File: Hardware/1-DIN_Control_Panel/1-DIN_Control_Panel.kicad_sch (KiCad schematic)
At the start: 13 parts

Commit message: Schematic progress
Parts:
- added J1: Conn_01x06, symbol Connector_Generic:Conn_01x06
- added J3: Pot/SW - Brightness, symbol Connector_Generic:Conn_01x05
- added U2: AD8603, Package_TO_SOT_SMD:TSOT-23-5, symbol Amplifier_Operational:AD8603
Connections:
- net GND: now also J3.3 (B); no longer J?.2 (Pin_2)
- net at J?.1 (Pin_1): no longer J?.2 (Pin_2) (x3)
- net VCC renamed +BATT
- net +BATT: now also J3.1 (A)
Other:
- moved on the sheet: J?

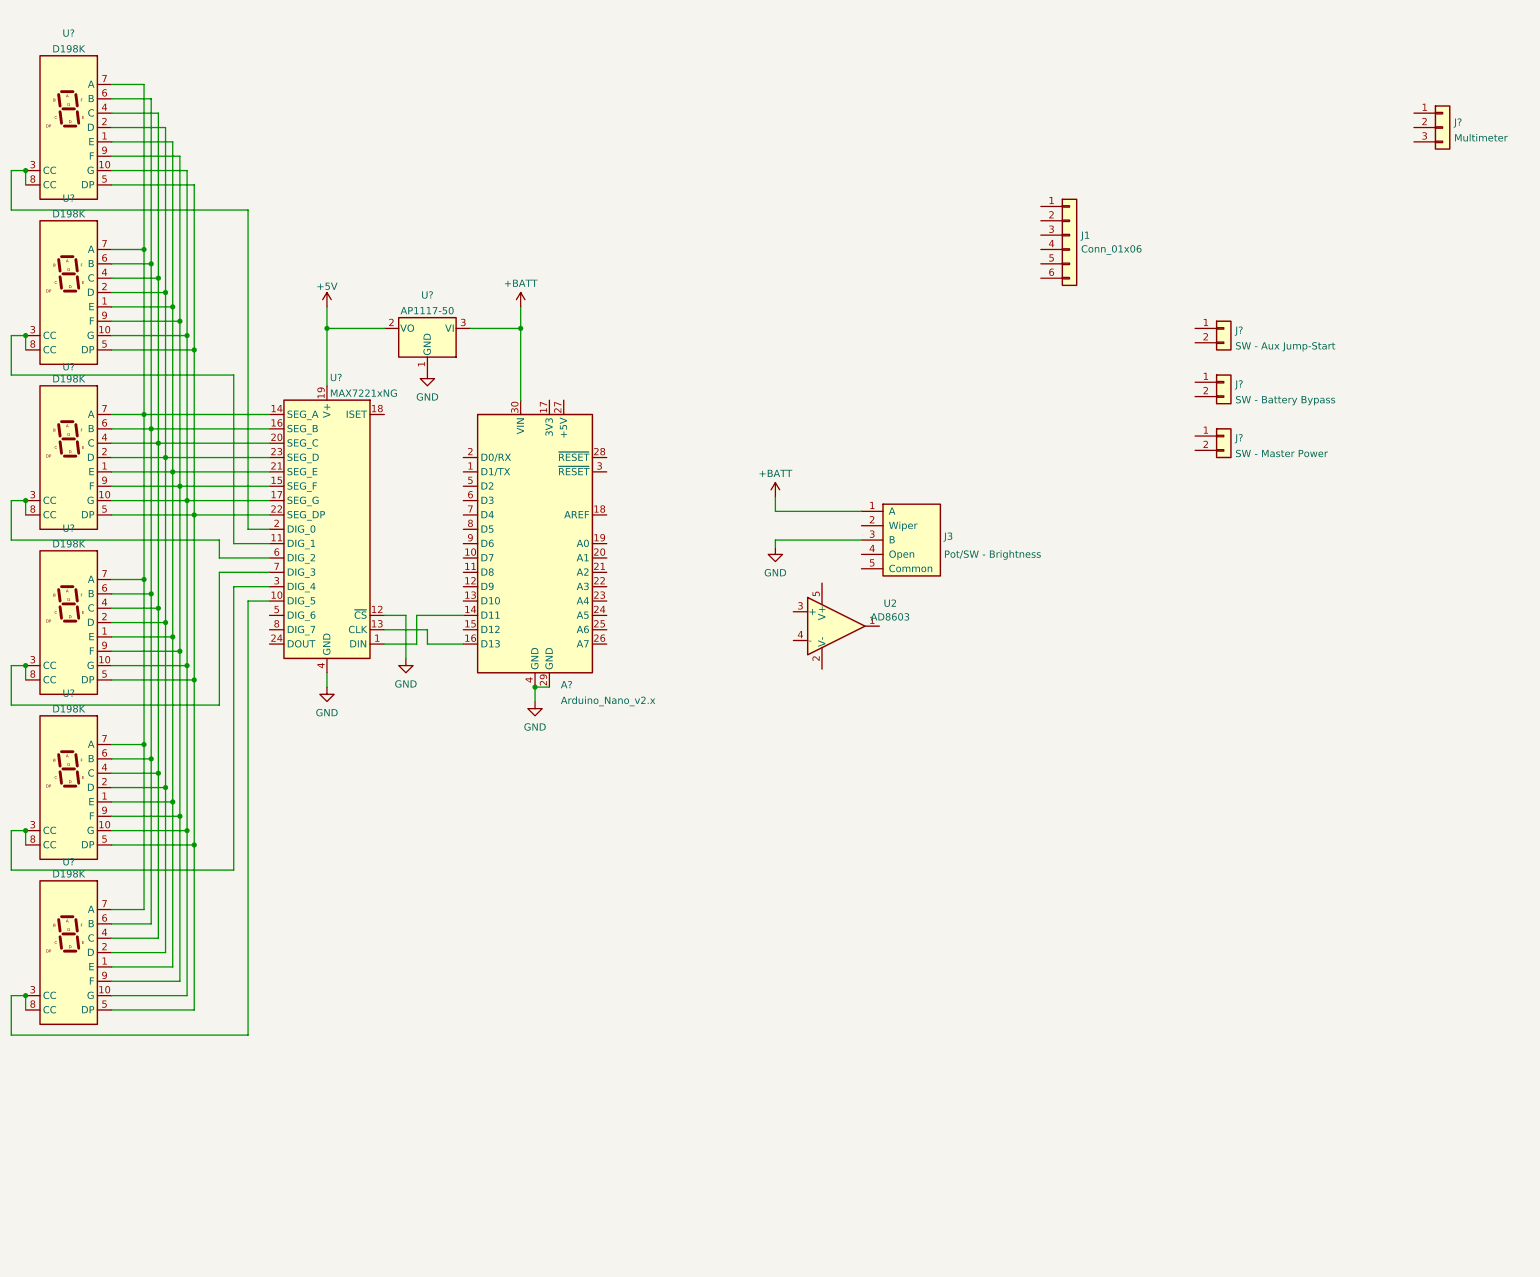
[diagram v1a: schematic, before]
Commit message: Added Instrumentation Amplifier To Schematic
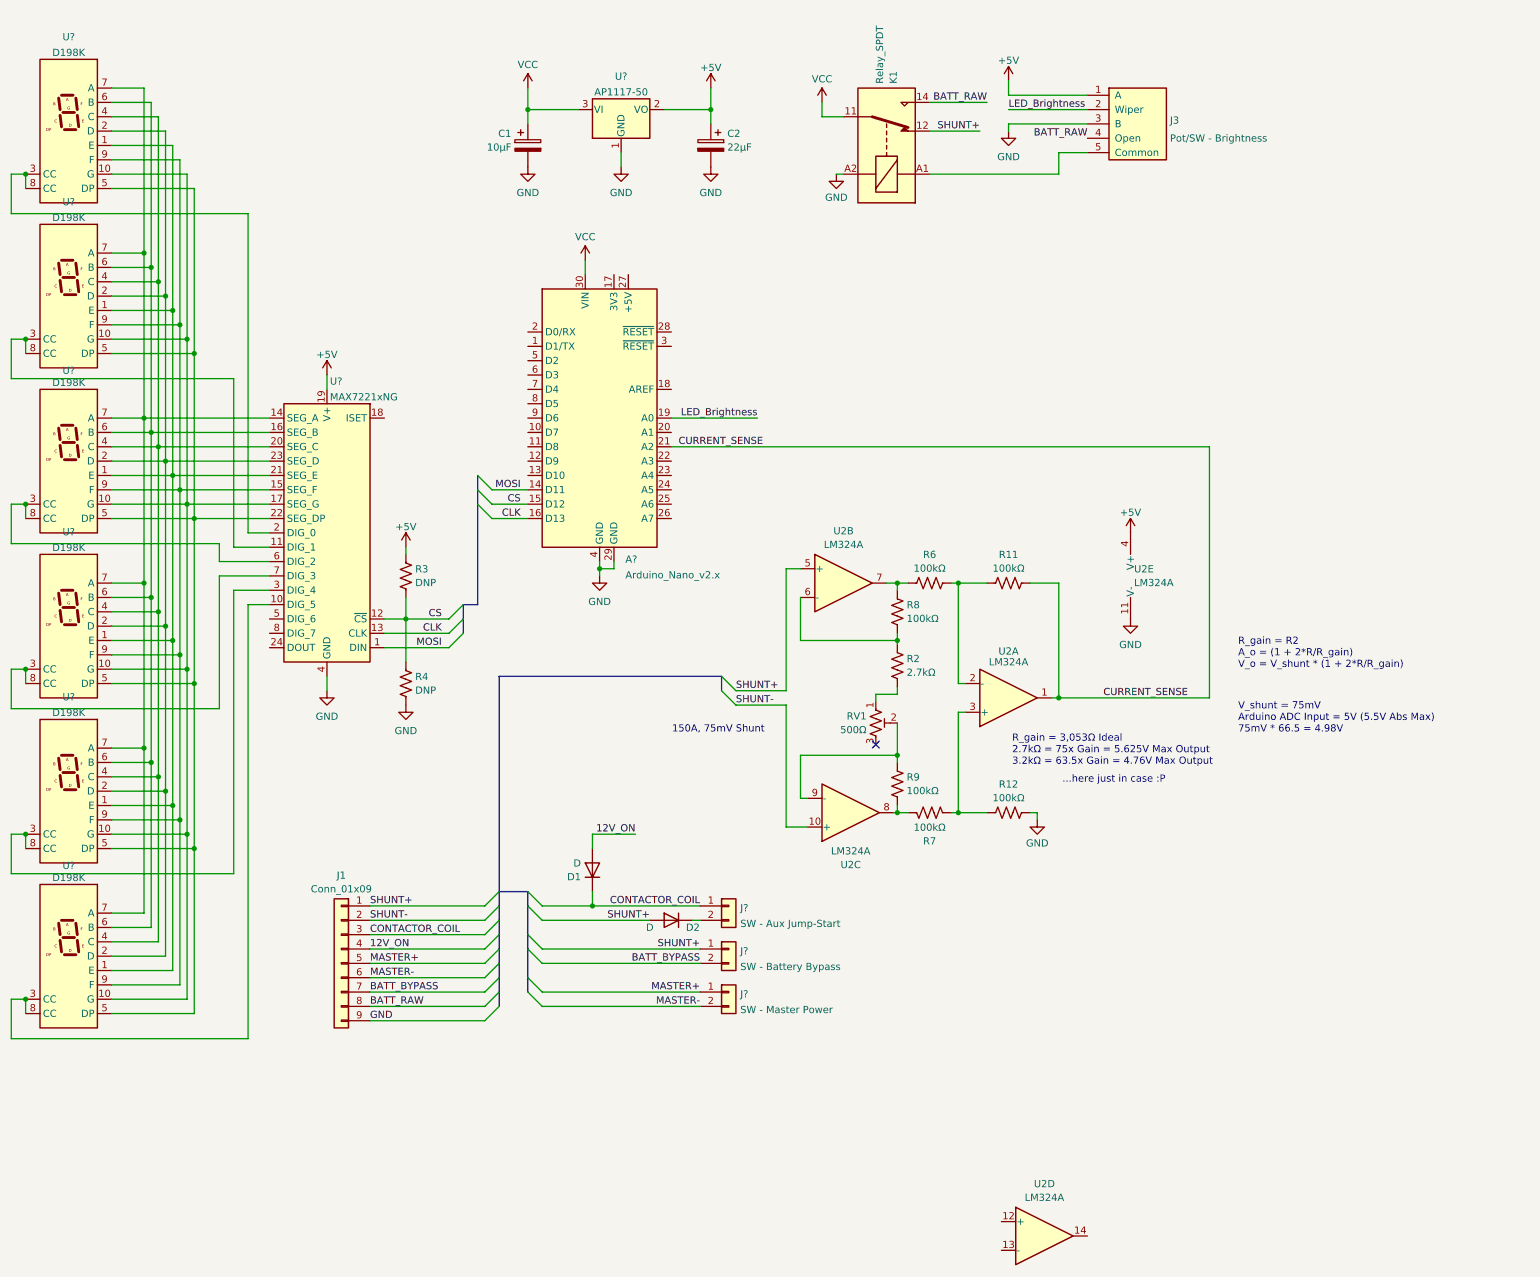
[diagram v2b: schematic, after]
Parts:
- removed J?: Multimeter, symbol Connector_Generic:Conn_01x03
- removed U2: AD8603, Package_TO_SOT_SMD:TSOT-23-5, symbol Amplifier_Operational:AD8603
- added C1: 10µF, symbol Device:C_Polarized
- added C2: 22µF, symbol Device:C_Polarized
- added D1, D2: D, symbol Device:D
- added K1: Relay_SPDT, symbol Relay:Relay_SPDT
- added R11, R12, R6, R7, R8, R9: 100kΩ, symbol Device:R_US
- added R2: 2.7kΩ, symbol Device:R_US
- added R3, R4: DNP, symbol Device:R_US
- added RV1: 500Ω, symbol Device:R_Potentiometer_Trim_US
- added U2: LM324A, symbol Amplifier_Operational:LM324A
- J1: value Conn_01x06 -> Conn_01x09; symbol Connector_Generic:Conn_01x06 -> Connector_Generic:Conn_01x09
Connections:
- net +5V: now also J3.1 (A), C2.1, R3.1, U2.4 (V+)
- net GND: now also J1.9 (Pin_9), C1.2, C2.2, K1.A2, R12.2, R4.2, U2.11 (V-); no longer U?.12 (~{CS})
- net SHUNT+: now reaches J1.1 (Pin_1)
- net SHUNT+: now also J?.1 (Pin_1), D2.2 (A), K1.12, U2.5 (+)
- net SHUNT-: now reaches J1.2 (Pin_2)
- net SHUNT-: now also U2.10 (+)
- net CONTACTOR_COIL: now reaches J1.3 (Pin_3)
- net CONTACTOR_COIL: now also J?.1 (Pin_1), D1.1 (K)
- net 12V_ON: now reaches J1.4 (Pin_4)
- net 12V_ON: now also D1.2 (A)
- net MASTER+: now reaches J1.5 (Pin_5)
- net MASTER+: now also J?.1 (Pin_1)
- net MASTER-: now reaches J1.6 (Pin_6)
- net MASTER-: now also J?.2 (Pin_2)
- net MOSI: now reaches A?.14 (D11), U?.1 (DIN)
- net CS: now reaches A?.15 (D12)
- net CS: now also U?.12 (~{CS}), R3.2, R4.1
- net CLK: now reaches A?.16 (D13), U?.13 (CLK)
- net LED_Brightness: now reaches A?.19 (A0)
- net LED_Brightness: now also J3.2 (Wiper)
- net CURRENT_SENSE: now reaches A?.21 (A2)
- net CURRENT_SENSE: now also R11.2, U2.1
- net BATT_BYPASS: now reaches J?.2 (Pin_2)
- net BATT_BYPASS: now also J1.7 (Pin_7)
- net at J?.2 (Pin_2): now also D2.1 (K)
- net BATT_RAW: now reaches J3.4 (Open)
- net BATT_RAW: now also J1.8 (Pin_8), K1.14
- net at J3.5 (Common): now also K1.A1
- net +BATT renamed VCC
- net VCC: now also C1.1, K1.11; no longer J3.1 (A)
- new net: R11.1, R6.2, U2.2 (-)
- new net: R12.1, R7.2, U2.3 (+)
- new net: R2.2, R8.1, U2.6 (-)
- new net: R6.1, R8.2, U2.7
- new net: R7.1, R9.1, U2.8
- new net: R9.2, RV1.2, U2.9 (-)
- new net: R2.1, RV1.1
- no-connect marks 0 -> 1
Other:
- note added: "...here just in case :P"
- note added: "150A, 75mV Shunt"
- note added: "R_gain = 3,053Ω Ideal 2.7kΩ = 75x Gain = 5.625V Max Output 3.2kΩ = 63.5x Gain = 4.76V Max Output"
- note added: "R_gain = R2 A_o = (1 + 2*R/R_gain) V_o = V_shunt * (1 + 2*R/R_gain)"
- note added: "V_shunt = 75mV Arduino ADC Input = 5V (5.5V Abs Max) 75mV * 66.5 = 4.98V"
- moved on the sheet: A?, J3, J?, U?
